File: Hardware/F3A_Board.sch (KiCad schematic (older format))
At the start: 10 parts, among them J1 Conn_01x03, U2 W25Q64V

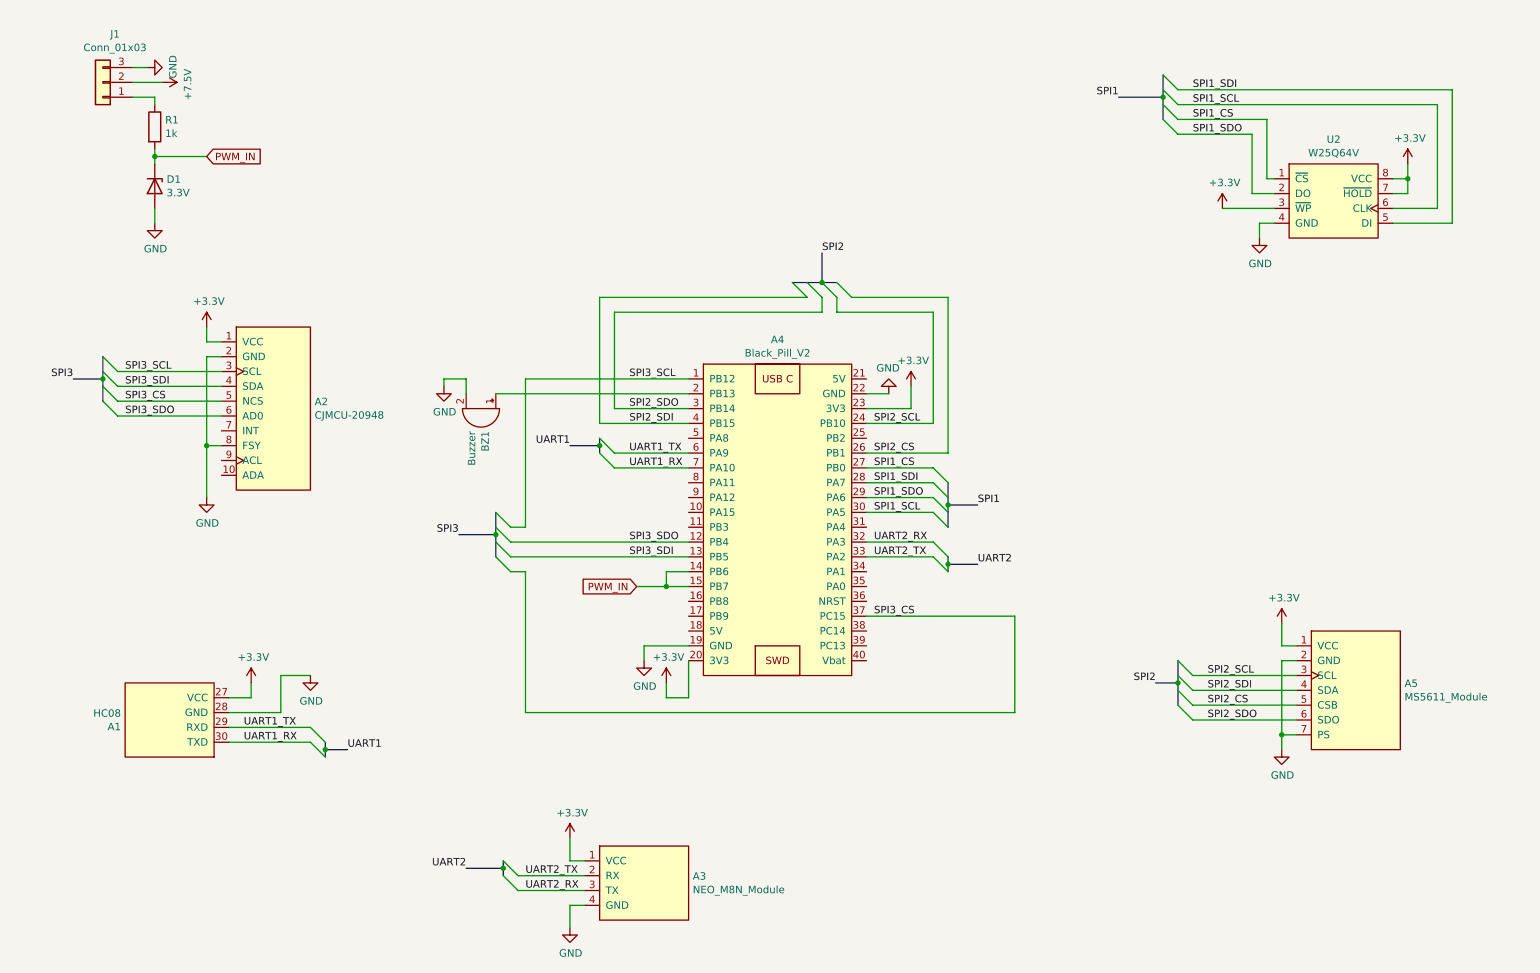
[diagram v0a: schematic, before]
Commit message: Adding Zener datasheets
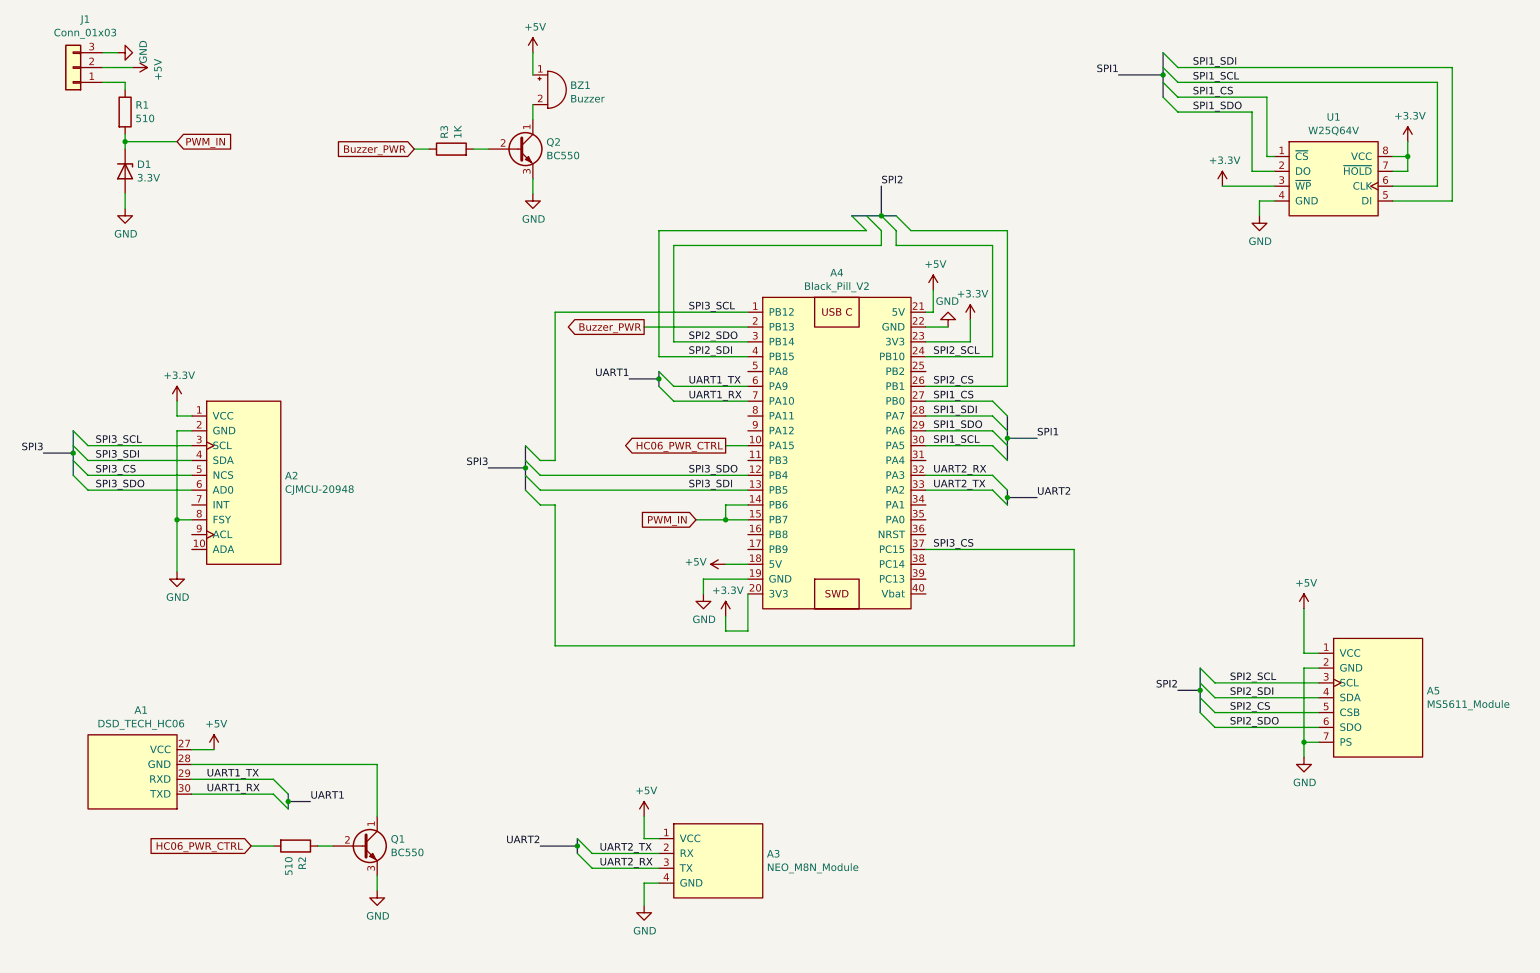
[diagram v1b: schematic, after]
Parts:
- removed A1: HC08, F3A_Modules:HC08, symbol F3A_Modules:HC08
- added A1: DSD_TECH_HC06, F3A_Modules:DSD_TECH_HC06, symbol F3A_Modules:DSD_TECH_HC06
- added Q1, Q2: BC550, Package_TO_SOT_THT:TO-92S_Wide, symbol Transistor_BJT:BC550
- added R2: 510, Resistor_THT:R_Axial_DIN0204_L3.6mm_D1.6mm_P7.62mm_Horizontal, symbol Device:R
- added R3: 1K, Resistor_THT:R_Axial_DIN0204_L3.6mm_D1.6mm_P7.62mm_Horizontal, symbol Device:R
- R1: value 1k -> 510
- renumbered U2 to U1
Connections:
- net +7.5V is gone; now on net +5V: J1.2 (Pin_2)
- net +3V3: no longer A3.1 (VCC), A5.1 (VCC)
- net GND: now also Q1.3 (E), Q2.3 (E); no longer BZ1.2 (+)
- net UART1_RX: now also A1.30 (TXD)
- net UART1_TX: now also A1.29 (RXD)
- net HC06_PWR_CTRL: now reaches A4.10 (PA15)
- net HC06_PWR_CTRL: now also R2.2
- net +5V: now reaches A4.18 (5V)
- net +5V: now also A3.1 (VCC), A4.21 (5V), A5.1 (VCC), BZ1.1 (-), A1.27 (VCC)
- net Buzzer_PWR: now reaches A4.2 (PB13)
- net Buzzer_PWR: now also R3.1; no longer BZ1.1 (-)
- new net: BZ1.2 (+), Q2.1 (C)
- new net: A1.28 (GND), Q1.1 (C)
- new net: Q1.2 (B), R2.1
- new net: Q2.2 (B), R3.2
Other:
- moved on the sheet: A2, A3, A4, A5, BZ1, D1, J1, R1, U1
